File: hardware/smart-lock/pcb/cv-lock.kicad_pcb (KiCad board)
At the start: 2 copper layers, 93.2 x 71.4 mm, 40 parts, among them J1 2P 5.08mm, J2 3P 5.08mm, J3 2P 2.54mm, K1 SRD-05VDC-SL-C, Q1 S8050, SW1 Tactile 6mm, U1 ESP32-WROOM-32E (4MB), U2 AMS1117-3.3, U3 MP1584 buck

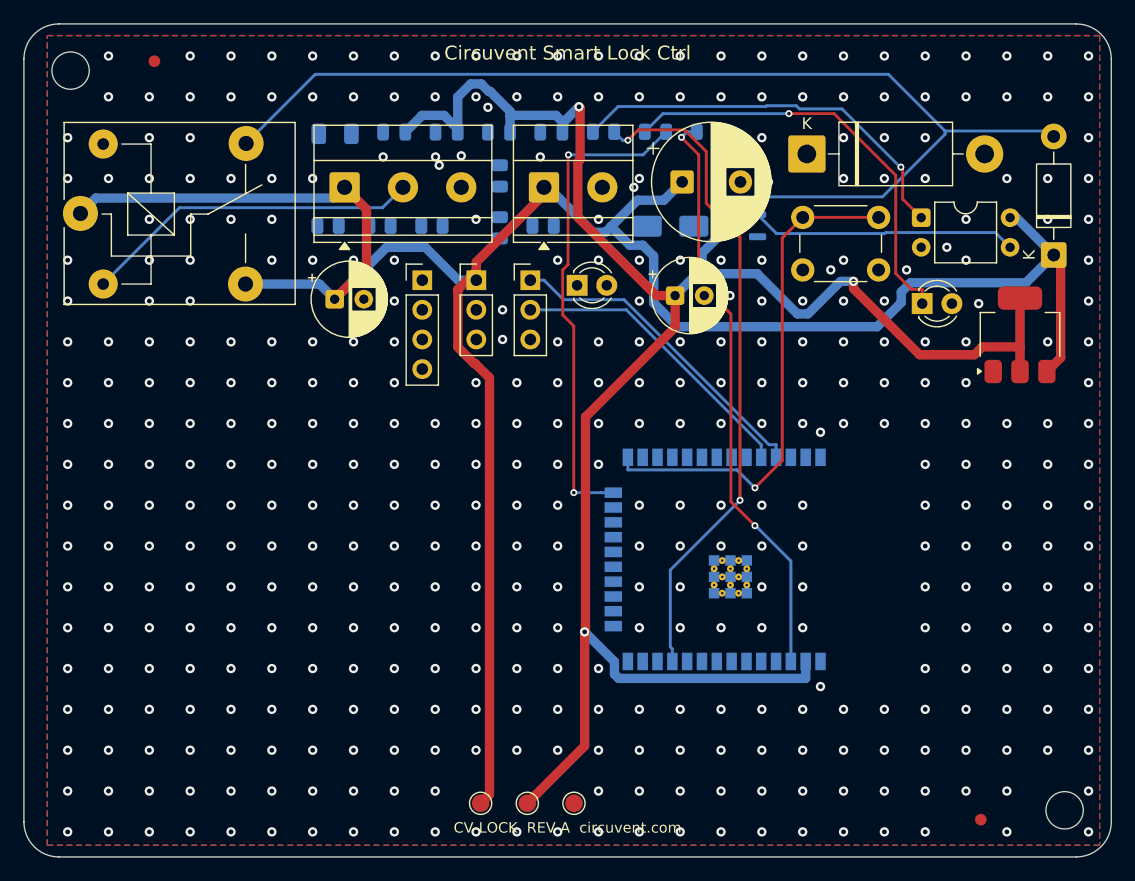
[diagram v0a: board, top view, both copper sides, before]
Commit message: hardware: fix mains isolation barrier gaps, add load-controller PCB
Adds the 13th board (ultra-compact dual-channel load controller: ESP32-C3,
opto+relay channel, MOSFET PWM channel, USB-C, AP2112K LDO, USBLC6 ESD) and
regenerates all 12 existing boards, which were stale with respect to earlier
relay-pinout and LED-polarity fixes.

The substantive change is to the mains isolation barrier. It is a keepout band
the router must not cross, deliberately cut where a component straddles it
because there the isolation is provided by the part's package. Three linked
defects made those cuts unsafe, each only visible once the previous was fixed:

1. The cut removed the barrier across the full band width for the straddling
   part's whole height, while the ISO_BRIDGE area that excuses the gap covered
   only the part itself. The router used the leftover strip beside the part to
   bring +5V within 6.99 mm of AC_N against an 8.0 mm reinforced creepage rule.
2. Straddling parts can overlap in y, so cutting per part put one part's
   keepout on another part's pads. The exempt x-ranges are now unioned per
   strip by a sweep line.
3. The rule only relaxes for items insideArea('ISO_BRIDGE'). With the hole the
   same size as the area, a track could hug the hole's edge without being
   contained in it, so the rule fired anyway and the router had no way to know.
   The hole is now the part's pad bbox + 0.3 mm, strictly inside ISO_BRIDGE at
   the footprint bbox + 0.6 mm.

The tighter hole leaves mains nets less room to reach bridge pads, so some
boards report more unconnected items. That is deliberate: those are documented
hand-routing items, whereas a creepage violation is a safety defect.

Also fixed in the generator:
- _pad_shape() derived a pad's layers from PAD::GetLayer(), which returns F.Cu
  even for pads on B.Cu. Every back-side pad became a phantom obstacle on the
  front, blocking legal paths there while hiding the real one behind. Only
  IsOnLayer() is truthful.
- Castella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
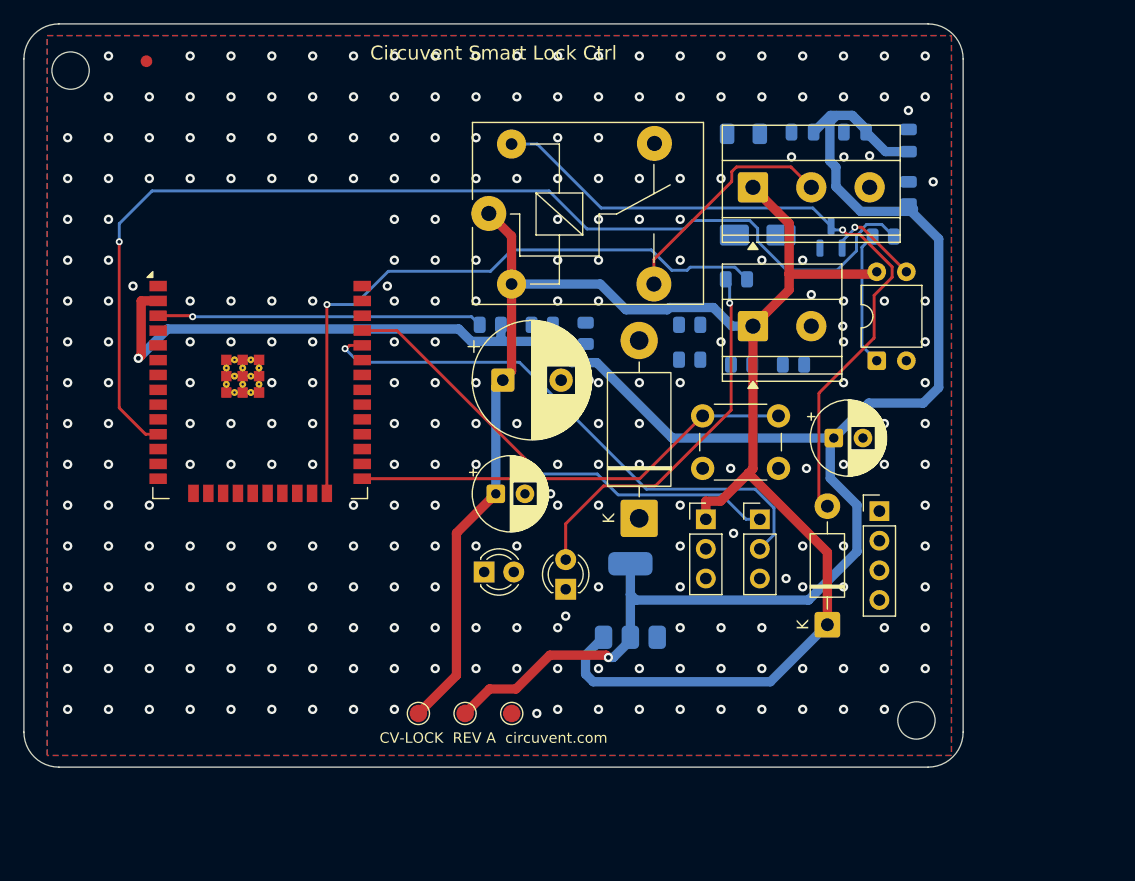
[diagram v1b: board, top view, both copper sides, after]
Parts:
- removed FID2: Fiducial, Fiducial_1mm_Mask2mm
- U1: moved to F.Cu
- U2: moved to B.Cu
- moved U1 46.5 mm to (120.2, 107.7), turned to 0 degrees
- moved U3 43.9 mm to (173.3, 121.8)
- moved U2 40.4 mm to (152.0, 129.4)
- moved LED1 39.2 mm to (146.4, 128.5), turned to 90 degrees
- moved D1 37.2 mm to (168.9, 131.5)
- moved C5 35.1 mm to (175.8, 90.0), turned to 90 degrees
- moved J2 35.0 mm to (162.5, 94.0)
- moved C4 35.0 mm to (171.2, 89.3)
- moved Csn 35.0 mm to (166.7, 89.3)
- moved K1 35.0 mm to (139.8, 96.2)
- moved F1 35.0 mm to (161.7, 89.4)
- moved D2 34.4 mm to (152.7, 122.4), turned to 90 degrees
- moved R6 32.1 mm to (157.1, 105.8)
- moved C6 31.0 mm to (175.8, 94.5), turned to 90 degrees
- moved R8 29.1 mm to (161.5, 109.2)
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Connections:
- K1 pad 2: LOCK_RELAY_SW -> +5V
- K1 pad 3: +5V -> LOCK_RELAY_SW
- K1 pad 4: LOCK_RELAY_COIL -> N$K1.4
- K1 pad 5: N$K1.5 -> LOCK_RELAY_COIL
- LED1 pad 1: LED_PIN_A -> GND
- LED1 pad 2: GND -> LED_PIN_A
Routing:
- net +5V: track 194.4 -> 152.9 mm
- net LOCK_RELAY: track 56.8 -> 94.5 mm, vias 2 -> 1
- net LOCK_RELAY_COIL: track 95.7 -> 60.4 mm, vias 0 -> 1
- net LOCK_RELAY_OPT: track 34.6 -> 11.5 mm, vias 1 -> 0
- net EN: track 50.3 -> 27.9 mm, vias 2 -> 1
- net UART_RX: track 25.7 -> 48.0 mm, vias 0 -> 1
- net LOCK_RELAY_DRV: track 22.9 -> 8.24 mm, vias 0 -> 1
- net LED_PIN: track 42.1 -> 55.4 mm, vias 2 -> 1
- net UART_TX: track 28.0 -> 40.9 mm, vias 0 -> 1
- net +3V3: track 171.1 -> 181.5 mm, vias 3 -> 2
- net LOCK_RELAY_SW: track 29.1 -> 20.1 mm
- net BTN_PIN: track 44.0 -> 37.9 mm, vias 1 -> 0
- net LED_PIN_A: track 36.8 -> 32.7 mm
- net GND: vias 422 -> 274
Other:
- board size 93.2 x 71.4 mm -> 80.5 x 63.7 mm

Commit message: Release 1.10.0, and stop shipping permissions the app never uses
Cut 1.10.0 (versionCode 12) and built it: AAB 38 MB, APK 83 MB, signed with the
upload key, JS bundle embedded.

Checking the generated manifest before writing the Play listing turned up
permissions no one had asked for. Every one of them is printed on the store page
for users to read before they install:

  RECORD_AUDIO          expo-camera asks for the microphone so video can be
                        recorded with sound. This app only ever puts the camera
                        in barcode mode to read a QR label, and expo-speech is
                        output-only - it speaks, it does not listen. Left in,
                        Play lists "Microphone" against a home-control app,
                        which is alarming, unexplainable and untrue.
  SYSTEM_ALERT_WINDOW   React Native's development overlay, useless in a release
                        build and shown to users as "Display over other apps".
  READ/WRITE_EXTERNAL_STORAGE
                        Legacy storage access nothing here touches.

Stripped via android.blockedPermissions. That emits tools:node="remove", which
is a merge instruction rather than a guarantee, so it was checked against the
finished artifact with aapt2 rather than the source manifest - all four are
absent from the APK.

NEARBY_WIFI_DEVICES now carries neverForLocation. Android otherwise treats it as
location-capable, because knowing which networks are in range is enough to place
someone, and Play's data safety review treats it the same way. The app uses it
only to join a new device's setup hotspot. That flag is a promise, so the plugin
says plainly that it has to come off if scan results are ever used positionally.

What is left is defensible: location for Wi-Fi onboarding (Android requires it),
camera for the QR label, nearby-devices flagged as non-positional.

Added mobile/store/listing with the text Play asks for - title, short and full
descriptions, and what'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
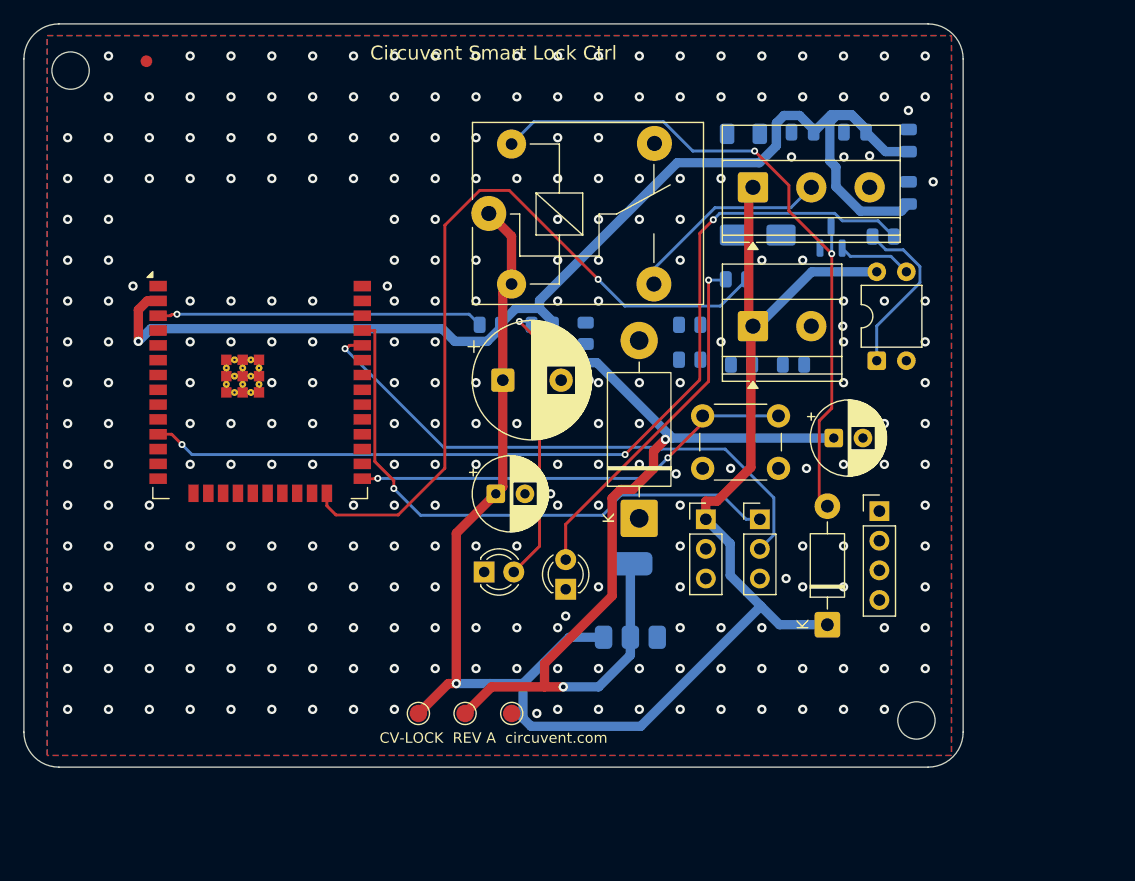
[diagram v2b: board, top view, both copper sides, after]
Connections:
- LED0 pad 1: N$LED0.1 -> GND
- LED0 pad 2: N$LED0.2 -> LED0_A
- R4 pad 1: N$R4.1 -> +3V3
- R4 pad 2: N$R4.2 -> LED0_A
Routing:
- net LED0_A: track 0.00 -> 24.3 mm, vias 0 -> 1
- net LOCK_RELAY: track 94.5 -> 80.5 mm, vias 1 -> 3
- net LED_PIN: track 55.4 -> 66.2 mm
- net UART_TX: track 40.9 -> 49.3 mm
- net +5V: track 152.9 -> 148.9 mm, vias 0 -> 1
- net LOCK_RELAY_OPT: track 11.5 -> 14.7 mm
- net LOCK_RELAY_SW: track 20.1 -> 17.7 mm
- net LED_PIN_A: track 32.7 -> 30.5 mm
- net LOCK_RELAY_DRV: track 8.24 -> 6.34 mm, vias 1 -> 0
- net LOCK_RELAY_COIL: track 60.4 -> 59.0 mm, vias 1 -> 2
- net +3V3: track 181.5 -> 182.3 mm, vias 2 -> 3
- net BTN_PIN: track 37.9 -> 38.3 mm, vias 0 -> 2
- net GND: vias 274 -> 273
